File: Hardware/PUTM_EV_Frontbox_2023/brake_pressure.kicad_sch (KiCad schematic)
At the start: 12 parts, among them U2 TLV9152IDDFR

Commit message: Added MCU wiring
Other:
- company: (none) -> Author: Szymon Kostrubiec
- title: (none) -> Brake pressure
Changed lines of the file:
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@@
 (kicad_sch (version 20230121) (generator eeschema)
   (paper "A4")
+  (title_block
+    (title "Brake pressure")
+    (date "2023-02-24")
+    (rev "${REVISION}")
+    (company "Author: Szymon Kostrubiec")
+    (comment 1 "Reviewer:")
+  )
   (junction (at 161.29 121.92) (diameter 0) (color 0 0 0 0)
   )

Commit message: Schematic ready for review
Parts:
- renumbered C27 to C29, R26 to R38, R27 to R39, R18 to R40, R22 to R41, R19 to R42, R23 to R43, R21 to R44, R24 to R45, R20 to R46, R25 to R47, U2 to U14
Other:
- note added: "All values TBD after selecting the sensor"
- moved on the sheet: R38, R39

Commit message: Fixed all issues
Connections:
- net +5V: no longer R38.1
- new net 5v_ref: R38.1
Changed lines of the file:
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@@
     (effects (font (size 1.27 1.27)) (justify left bottom))
+  )
+  (global_label "5v_ref" (shape input) (at 85.09 93.98 0) (fields_autoplaced)
+    (effects (font (size 1.27 1.27)) (justify left))
+    (property "Intersheetrefs" "${INTERSHEET_REFS}" (at 93.741 93.98 0)
+      (effects (font (size 1.27 1.27)) (justify left) hide)
+    )
   )
   (hierarchical_label "Brake_pressure_out_1" (shape output) (at 162.56 82.55 0) (fields_autoplaced)
@@
         )
       )
-    )
-  )
-  (symbol (lib_id "power:+5V") (at 85.09 93.98 0) (mirror y) (unit 1)
-    (in_bom yes) (on_board yes) (dnp no) (fields_autoplaced)
-    (property "Reference" "#PWR098" (at 85.09 97.79 0)
-      (effects (font (size 1.27 1.27)) hide)
-    )
-    (property "Value" "+5V" (at 85.09 90.17 0)
-      (effects (font (size 1.27 1.27)))
-    )
-    (property "Footprint" "" (at 85.09 93.98 0)
-      (effects (font (size 1.27 1.27)) hide)
-    )
-    (property "Datasheet" "" (at 85.09 93.98 0)
-      (effects (font (size 1.27 1.27)) hide)
-    )
-    (pin "1")
-    (instances
-      (project "PUTM_EV_Frontbox_2023"
-        (path "/b652b05a-4e3d-4ad1-b032-18886abe7d45/55cf8599-7fcf-4ad3-afe8-d836ab083f74"
-          (reference "#PWR098") (unit 1)
-        )
-      )

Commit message: Schematic modified, footprints assigned
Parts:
- C29: footprint (none) -> Capacitor_SMD:C_0402_1005Metric_Pad0.74x0.62mm_HandSolder
- R38, R39, R40, R41, R42, R43, R44, R45, R46, R47: footprint (none) -> Resistor_SMD:R_0402_1005Metric
- U14: footprint (none) -> Package_TO_SOT_SMD:TSOT-23-8_HandSoldering
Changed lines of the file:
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@@
       (effects (font (size 1.27 1.27)) (justify left))
     )
-    (property "Footprint" "" (at 143.51 93.98 0)
+    (property "Footprint" "Resistor_SMD:R_0402_1005Metric" (at 143.51 93.98 0)
       (effects (font (size 1.27 1.27)) hide)
     )
@@
       (effects (font (size 1.27 1.27)) (justify left))
     )
-    (property "Footprint" "" (at 132.08 83.82 0)
+    (property "Footprint" "Resistor_SMD:R_0402_1005Metric" (at 132.08 83.82 0)
       (effects (font (size 1.27 1.27)) hide)
     )
@@
       (effects (font (size 1.27 1.27)) (justify left))
     )
-    (property "Footprint" "" (at 132.08 123.19 0)
+    (property "Footprint" "Resistor_SMD:R_0402_1005Metric" (at 132.08 123.19 0)
       (effects (font (size 1.27 1.27)) hide)
     )
@@
       (effects (font (size 1.27 1.27)))
     )
-    (property "Footprint" "" (at 125.73 80.01 0)
+    (property "Footprint" "Resistor_SMD:R_0402_1005Metric" (at 125.73 80.01 0)
       (effects (font (size 1.27 1.27)) hide)
     )
@@
       (effects (font (size 1.27 1.27)))
     )
-    (property "Footprint" "" (at 152.4 82.55 0)
+    (property "Footprint" "Package_TO_SOT_SMD:TSOT-23-8_HandSoldering" (at 152.4 82.55 0)
       (effects (font (size 1.27 1.27)) hide)
     )
@@
       (effects (font (size 1.27 1.27)))
     )
-    (property "Footprint" "" (at 125.73 119.38 0)
+    (property "Footprint" "Resistor_SMD:R_0402_1005Metric" (at 125.73 119.38 0)
       (effects (font (size 1.27 1.27)) hide)
     )
@@
       (effects (font (size 1.27 1.27)) (justify left))
     )
-    (property "Footprint" "" (at 85.09 105.41 0)
+    (property "Footprint" "Resistor_SMD:R_0402_1005Metric" (at 85.09 105.41 0)
       (effects (font (size 1.27 1.27)) hide)
     )
@@
       (effects (font (size 1.27 1.27)) (justify left))
     )
-    (property "Footprint" "" (at 143.51 133.35 0)
+    (property "Footprint" "Resistor_SMD:R_0402_1005Metric" (at 143.51 133.35 0)
       (effects (font (size 1.27 1.27)) hide)
     )
@@
       (effects (font (size 1.27 1.27)) (justify left))
     )
-    (property "Footprint" "" (at 196.85 101.6 0)
+    (property "Footprint" "Capacitor_SMD:C_0402_1005Metric_Pad0.74x0.62mm_HandSolder" (at 196.85 101.6 0)
       (effects (font (size 1.27 1.27)) hide)
     )
@@
       (effects (font (size 1.27 1.27)))
     )
-    (property "Footprint" "" (at 151.13 90.17 0)
+    (property "Footprint" "Resistor_SMD:R_0402_1005Metric" (at 151.13 90.17 0)
       (effects (font (size 1.27 1.27)) hide)
     )
@@
       (effects (font (size 1.27 1.27)))
     )
-    (property "Footprint" "" (at 151.13 129.54 0)
+    (property "Footprint" "Resistor_SMD:R_0402_1005Metric" (at 151.13 129.54 0)
       (effects (font (size 1.27 1.27)) hide)
     )
@@
       (effects (font (size 1.27 1.27)) (justify left))
     )
-    (property "Footprint" "" (at 85.09 97.79 0)
+    (property "Footprint" "Resistor_SMD:R_0402_1005Metric" (at 85.09 97.79 0)
       (effects (font (size 1.27 1.27)) hide)
     )
@@
       (effects (font (size 1.27 1.27)))
     )
-    (property "Footprint" "" (at 152.4 121.92 0)
+    (property "Footprint" "Package_TO_SOT_SMD:TSOT-23-8_HandSoldering" (at 152.4 121.92 0)
       (effects (font (size 1.27 1.27)) hide)
     )
@@
       (effects (font (size 1.27 1.27)) (justify left))
     )
-    (property "Footprint" "" (at 204.47 101.6 0)
-      (effects (font (size 1.27 1.27)) hide)
-    )
+    (property "Footprint" "Package_TO_SOT_SMD:TSOT-23-8_HandSoldering" (at 204.47 101.6 0)
+      (effects (font (size 1.27 1.27)) hide)
+    )

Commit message: PCB taken apart
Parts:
- removed C29: 100n, Capacitor_SMD:C_0402_1005Metric_Pad0.74x0.62mm_HandSolder, symbol Device:C_Small
- removed R38, R39, R40, R41, R42, R43, R44, R45, R46, R47: R_Small, Resistor_SMD:R_0402_1005Metric, symbol Device:R_Small
- removed U14: TLV9152IDDFR, Package_TO_SOT_SMD:TSOT-23-8_HandSoldering, symbol Amplifier_Operational:TLV9062
- added C29: 100n, Capacitor_SMD:C_0603_1608Metric_Pad1.08x0.95mm_HandSolder, symbol Device:C
- added R48, R51 (x2): 0R, Resistor_SMD:R_0603_1608Metric_Pad0.98x0.95mm_HandSolder, symbol Device:R
- added R49, R50: 100R, Resistor_SMD:R_0603_1608Metric_Pad0.98x0.95mm_HandSolder, symbol Device:R
- added R51: 3k3, Resistor_SMD:R_0603_1608Metric_Pad0.98x0.95mm_HandSolder, symbol Device:R
- added RV3: 2k, Potentiometer_SMD:Potentiometer_Bourns_3214J_Horizontal, symbol Device:R_Potentiometer_Small
- added TP14: BR_N, TestPoint:TestPoint_Pad_D1.0mm, symbol Connector:TestPoint
- added TP15: BR_P, TestPoint:TestPoint_Pad_D1.0mm, symbol Connector:TestPoint
- added TP16: BR_MID, TestPoint:TestPoint_Pad_D1.0mm, symbol Connector:TestPoint
- added TP17: BR_OUT, TestPoint:TestPoint_Pad_D1.0mm, symbol Connector:TestPoint
- added U2: MCP6002-xMC, Package_DFN_QFN:DFN-8-1EP_3x2mm_P0.5mm_EP1.7x1.4mm, symbol Amplifier_Operational:MCP6002-xMC
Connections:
- net +5V: now also RV3.1
- net GND: now also C29.2, R50.1, R51.2, RV3.3, U2.4 (V-), U2.9 (V-)
- new net: R51.1, TP16.1, U2.3 (+), U2.7
- new net: R48.1, R50.2, TP15.1, U2.5 (+)
- new net: R49.1, R51.2, TP14.1, U2.6 (-)
- new net: R49.2, RV3.2
- new net: R51.1, R51.2, U2.2 (-)
- new net +3V3: C29.1, U2.8 (V+)
- new net IN: R48.2
- new net OUT: R51.1, TP17.1, U2.1
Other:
- note added: "0.5 V"
- note added: "0.5 to 2.4 V"
- note removed: "All values TBD after selecting the sensor"

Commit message: Routing
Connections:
- net +3V3 renamed +3.3VA
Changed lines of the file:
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@@
     )
   )
-  (symbol (lib_id "power:+3V3") (at 214.63 84.455 0) (unit 1)
-    (in_bom yes) (on_board yes) (dnp no) (fields_autoplaced)
-    (property "Reference" "#PWR017" (at 214.63 88.265 0)
+  (symbol (lib_id "power:+3.3VA") (at 214.63 84.455 0) (unit 1)
+    (in_bom yes) (on_board yes) (dnp no)
+    (property "Reference" "#PWR?" (at 214.63 88.265 0)
       (effects (font (size 1.27 1.27)) hide)
     )
-    (property "Value" "+3V3" (at 214.63 80.645 0)
+    (property "Value" "+3.3VA" (at 214.63 79.375 0)
       (effects (font (size 1.27 1.27)))
     )
@@
     (instances
       (project "PUTM_EV_Frontbox_2023"
+        (path "/b652b05a-4e3d-4ad1-b032-18886abe7d45"
+          (reference "#PWR?") (unit 1)
+        )
+        (path "/b652b05a-4e3d-4ad1-b032-18886abe7d45/911b86f7-6c1b-4cf5-8c52-4f515716b2b9"
+          (reference "#PWR0109") (unit 1)
+        )
+        (path "/b652b05a-4e3d-4ad1-b032-18886abe7d45/cff9e037-b571-49da-8ef7-9a05892cc423"
+          (reference "#PWR064") (unit 1)
+        )
+        (path "/b652b05a-4e3d-4ad1-b032-18886abe7d45/9be5e515-3e18-403e-b27a-ea3087f1514f"
+          (reference "#PWR0166") (unit 1)
+        )
+        (path "/b652b05a-4e3d-4ad1-b032-18886abe7d45/9e566fb6-1741-4092-b17e-402796433191"
+          (reference "#PWR0177") (unit 1)
+        )
         (path "/b652b05a-4e3d-4ad1-b032-18886abe7d45/a44ca1e3-5a7e-4627-a097-706c52508f74"
           (reference "#PWR017") (unit 1)
@@
         )
       )
-      (project "apps"
-        (path "/fc4ad874-c922-4070-89f9-7262080469d8/00000000-0000-0000-0000-00005f60f829"
-          (reference "#PWR062") (unit 1)
-        )
-        (path "/fc4ad874-c922-4070-89f9-7262080469d8/347af574-7f04-42ac-a8b1-78f5ed89add6"
-          (reference "#PWR069") (unit 1)
-        )
-        (path "/fc4ad874-c922-4070-89f9-7262080469d8/11236715-9d3d-46a6-8693-03c5fb52ffb8"
-          (reference "#PWR070") (unit 1)
-        )
-        (path "/fc4ad874-c922-4070-89f9-7262080469d8/dfb38113-578c-49b0-8230-ef742c26f2e9"
-          (reference "#PWR077") (unit 1)
-        )
-        (path "/fc4ad874-c922-4070-89f9-7262080469d8/0b6b627a-962c-42da-9dc9-8c53f83f5a9f"
-          (reference "#PWR077") (unit 1)
-        )
-        (path "/fc4ad874-c922-4070-89f9-7262080469d8/92bd39b8-75fd-4234-bc33-f3cbcd27f008"
-          (reference "#PWR077") (unit 1)
-        )
-      )

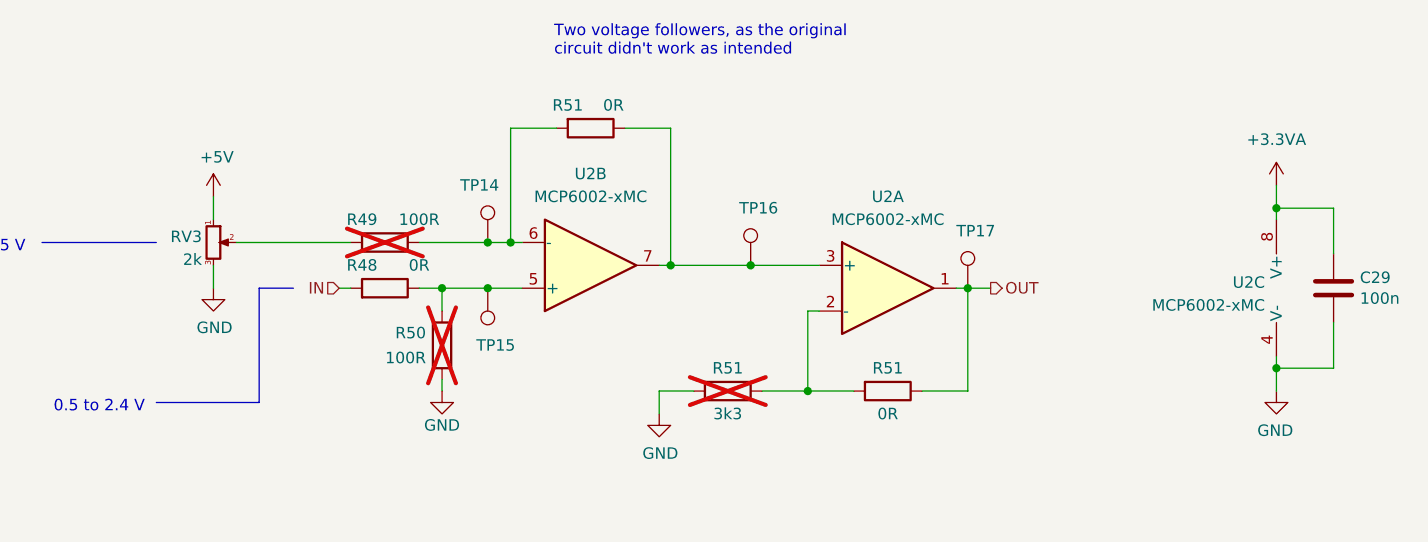
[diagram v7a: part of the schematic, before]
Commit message: Added gearbox temperature sensors on schematic
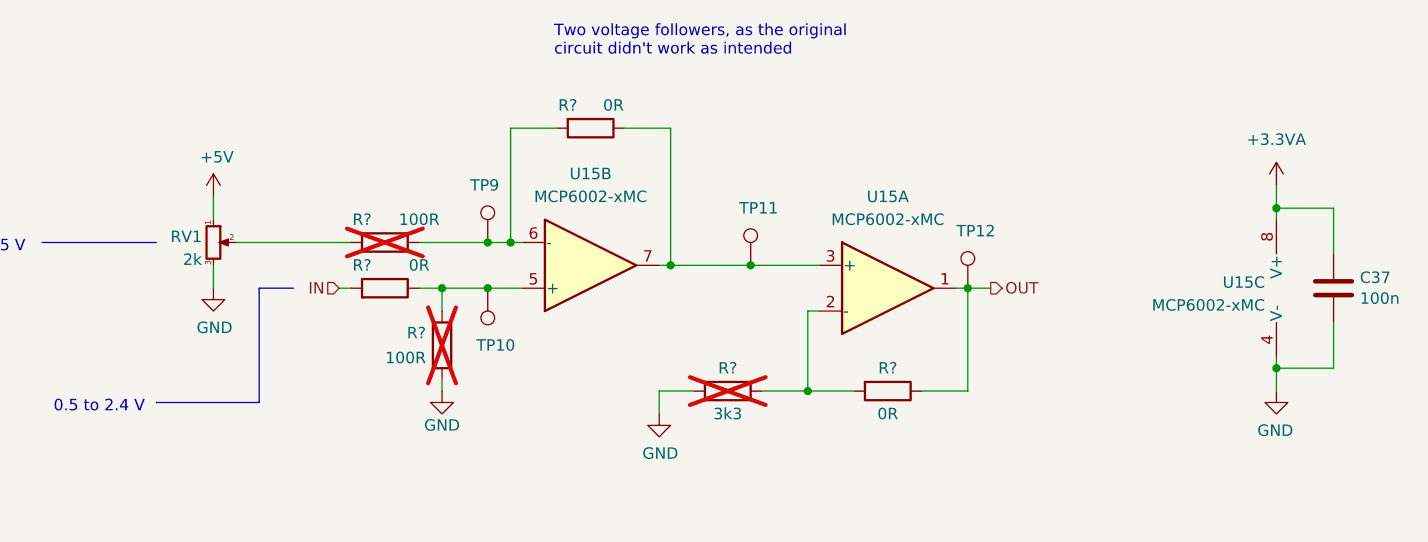
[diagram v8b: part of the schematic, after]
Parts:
- renumbered C29 to C37, R50 to R?, R49 to R?, R48 to R?, R51 to R?, RV3 to RV1, TP15 to TP10, TP16 to TP11, TP17 to TP12, TP14 to TP9, U2 to U15
